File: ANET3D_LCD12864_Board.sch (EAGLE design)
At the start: 14 parts, among them J1 J3, Q5 BC817, SW1 RESET, U1 (DNP)

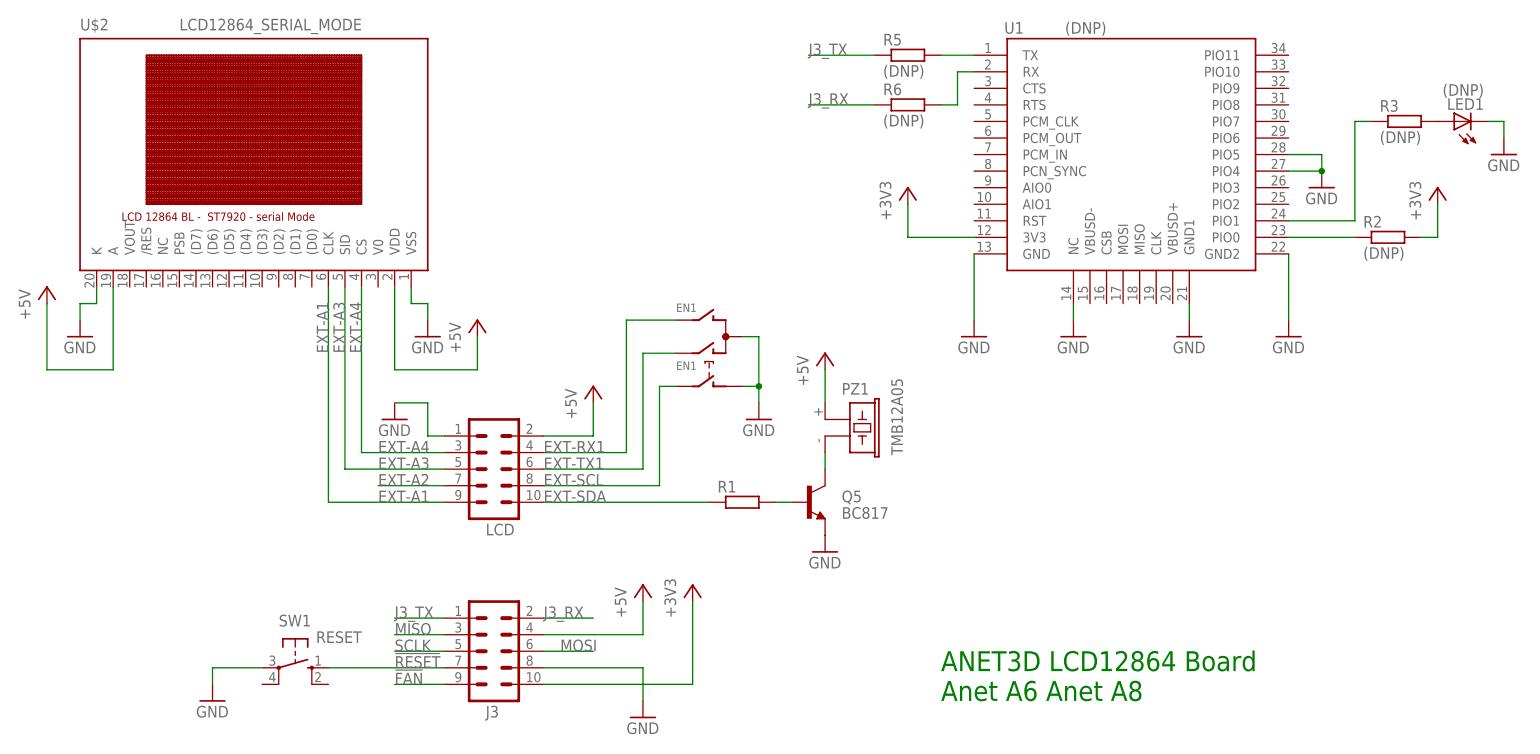
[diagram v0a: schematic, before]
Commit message: value R31 corrected
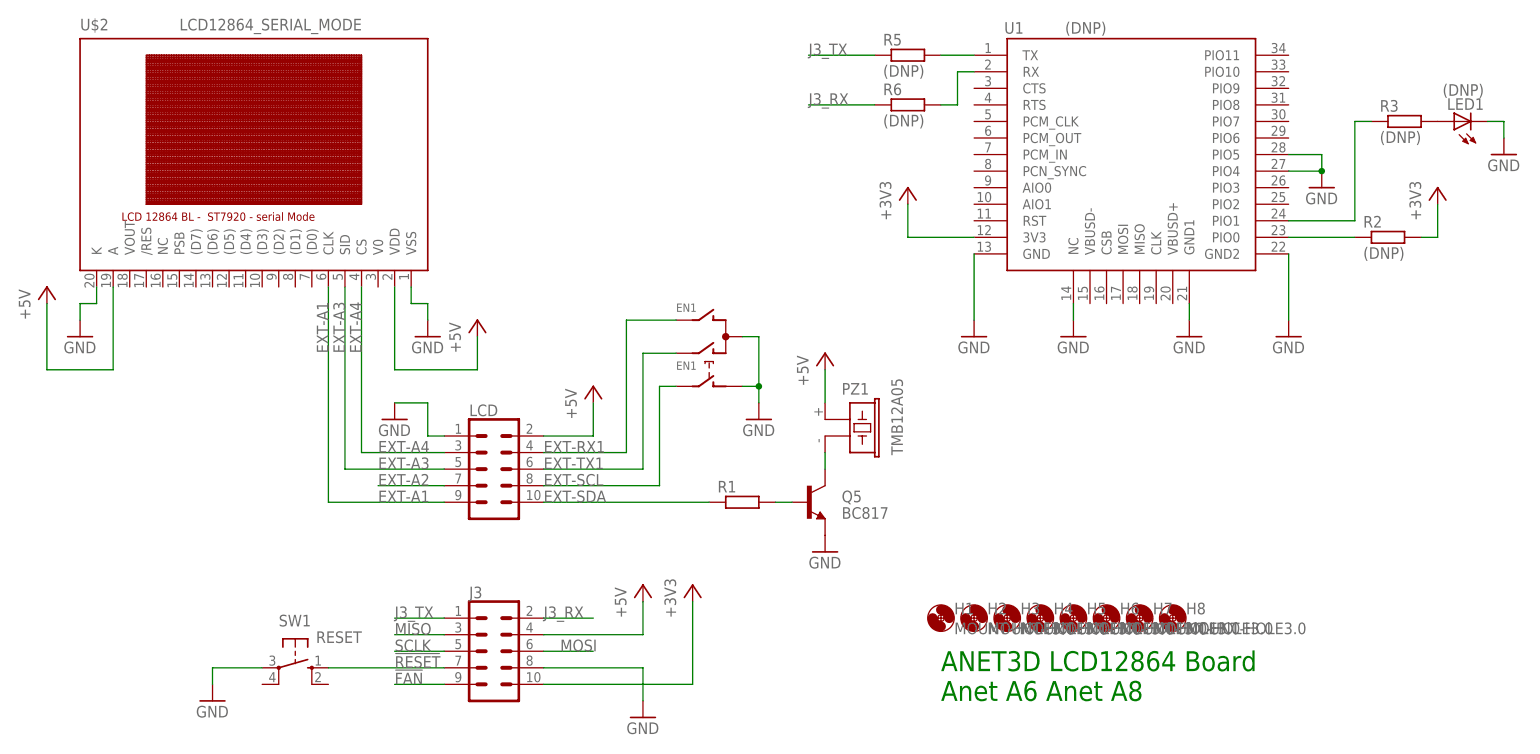
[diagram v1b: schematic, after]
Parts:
- removed J1: J3, con-harting-ml:ML10
- removed LCD1: LCD, con-harting-ml:ML10
- added H1, H2, H3, H4, H5, H6, H7, H8: MOUNT-HOLE3.0, holes:MOUNT-HOLE3.0
- added J3, LCD: (no value), SparkFun-Connectors:CONN_05X2SHD_SMD
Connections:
- net !FAN: now also J3.9; no longer J1.9
- net !RESET: now also J3.7; no longer J1.7
- net +3V3: now also J3.10; no longer J1.10
- net +5V: now also J3.4, LCD.2; no longer J1.4, LCD1.2
- net EXT-A1: now also LCD.9; no longer LCD1.9
- net EXT-A2: now also LCD.7; no longer LCD1.7
- net EXT-A3: now also LCD.5; no longer LCD1.5
- net EXT-A4: now also LCD.3; no longer LCD1.3
- net EXT-RX1: now also LCD.4; no longer LCD1.4
- net EXT-SCL: now also LCD.8; no longer LCD1.8
- net EXT-SDA: now also LCD.10; no longer LCD1.10
- net EXT-TX1: now also LCD.6; no longer LCD1.6
- net GND: now also J3.8, LCD.1; no longer J1.8, LCD1.1
- net J3_RX: now also J3.2; no longer J1.2
- net J3_TX: now also J3.1; no longer J1.1
- net MISO: now also J3.3; no longer J1.3
- net MOSI: now also J3.6; no longer J1.6
- net SCLK: now also J3.5; no longer J1.5
